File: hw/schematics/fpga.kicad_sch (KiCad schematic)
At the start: 34 parts, among them U3 ICE40UL1K-CM36AITR

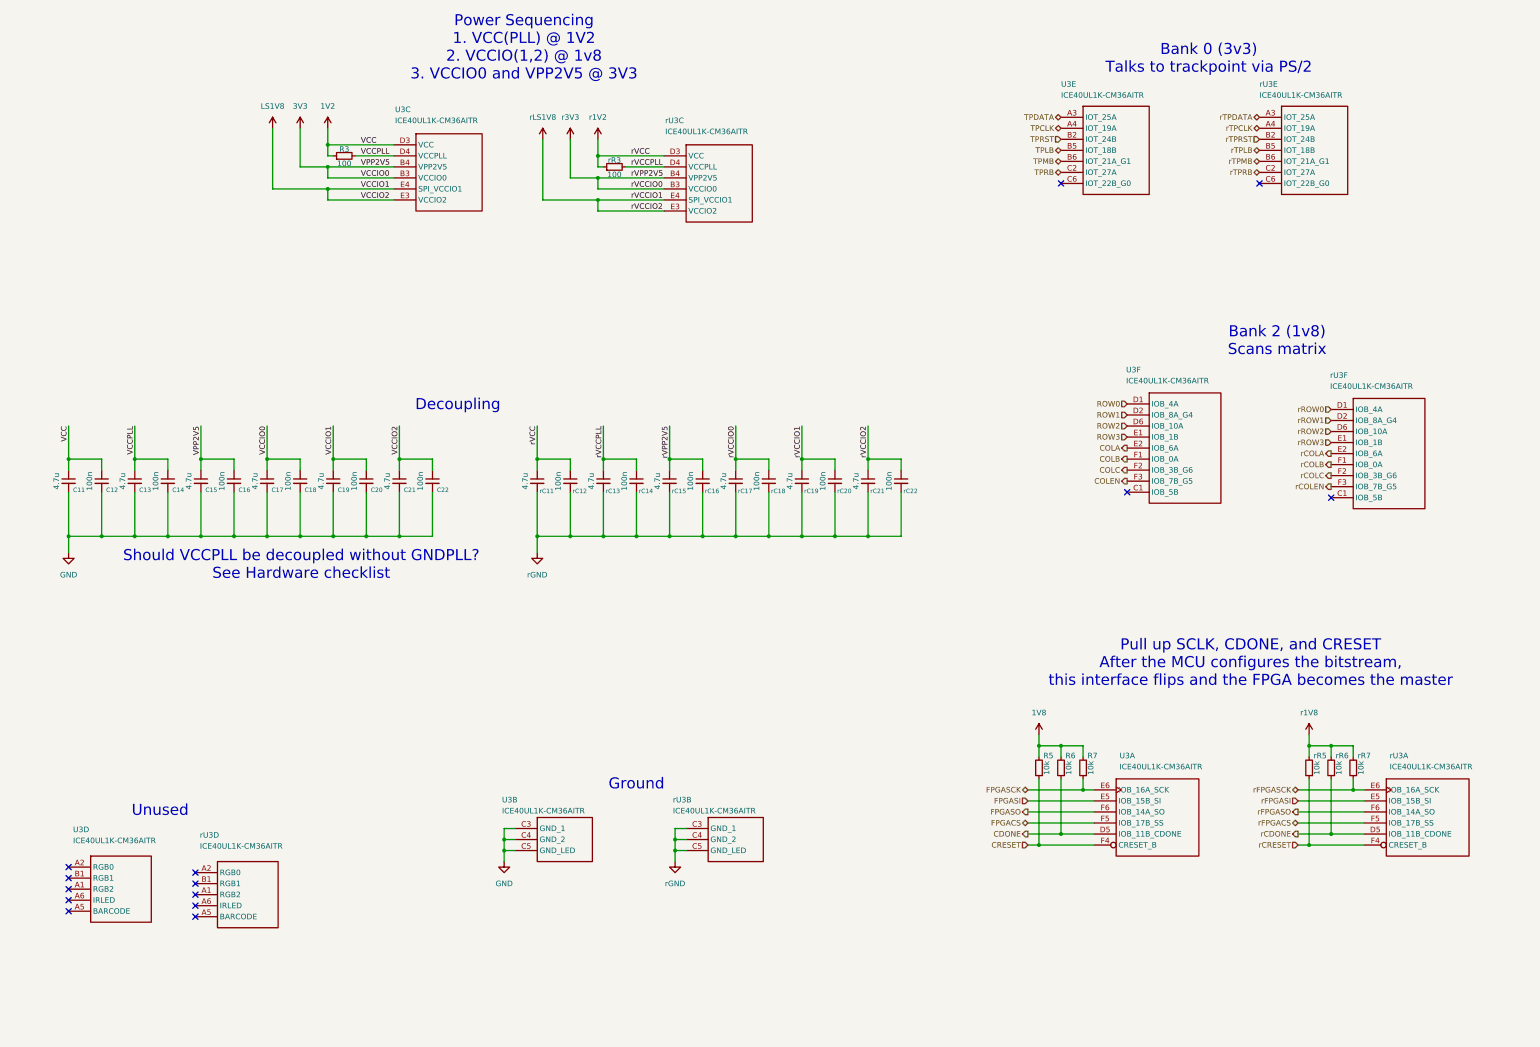
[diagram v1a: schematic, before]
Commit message: Use ICE40UP instead of UL
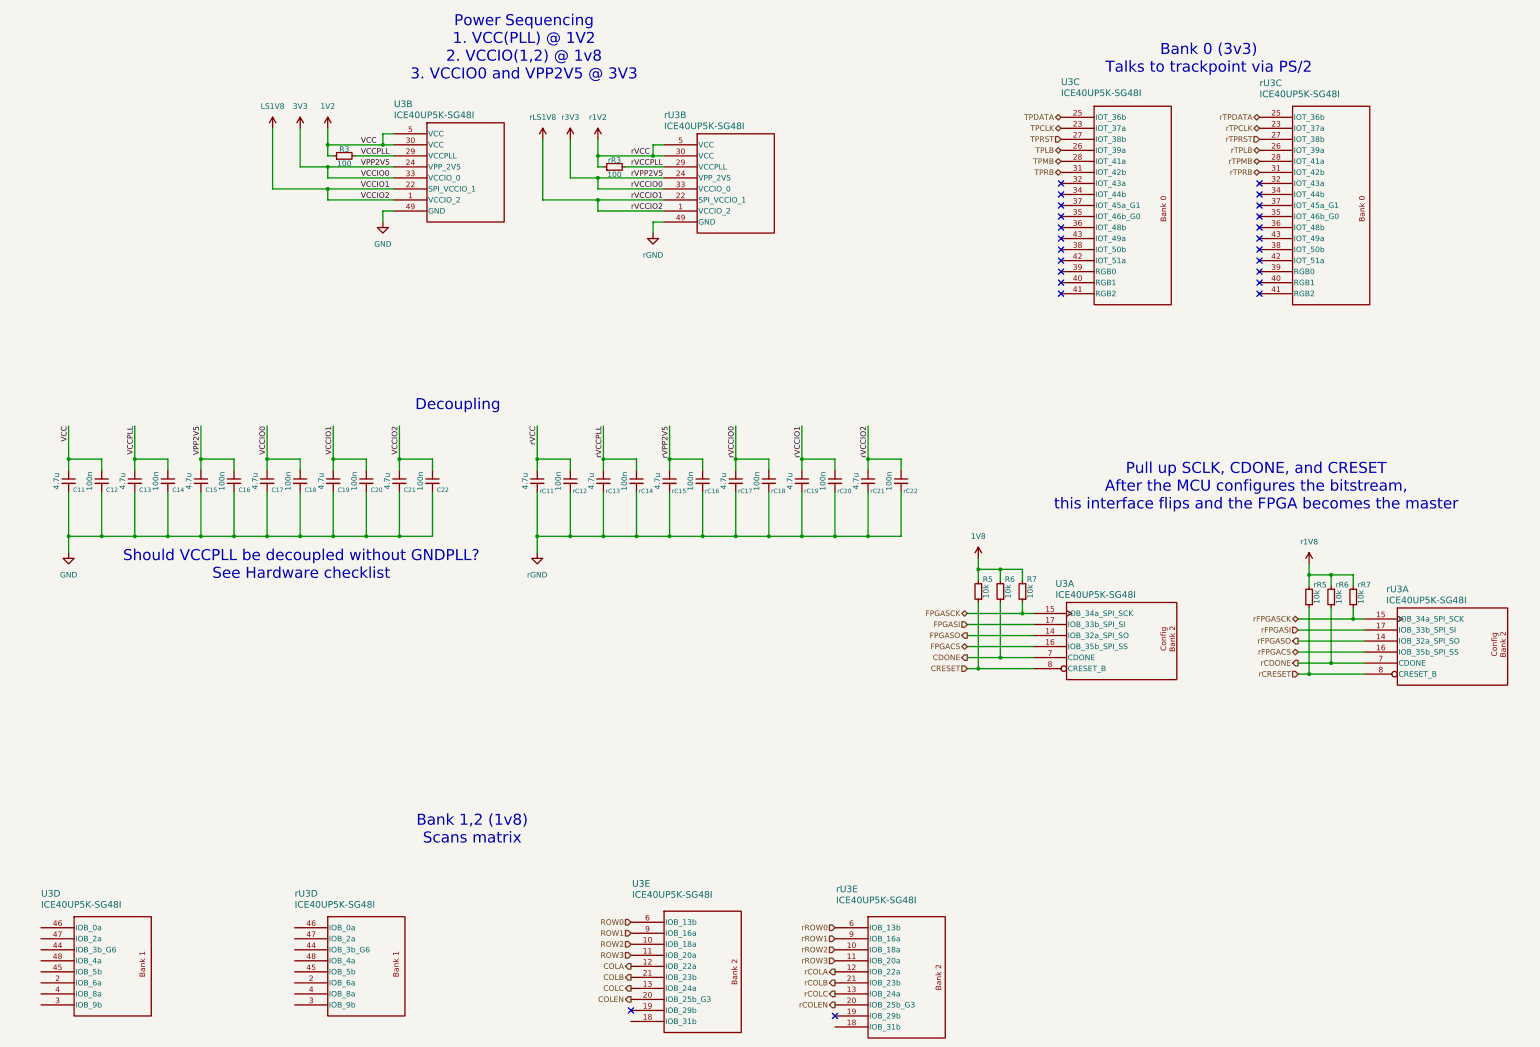
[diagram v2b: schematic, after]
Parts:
- removed U3, rU3: ICE40UL1K-CM36AITR, Alidade:BGA36C40P6X6_250X250X100, symbol Alidade:ICE40UL1K-CM36AITR
- added U3, rU3: ICE40UP5K-SG48I, Alidade:QFN48_L-ASC10_ICE40ULTRAPLUS_MACHXO2_LAT, symbol Alidade:ICE40UP5K-SG48I
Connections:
- net 1V2: now also U3.30 (VCC), U3.5 (VCC)
- net 3V3: now also U3.24 (VPP_2V5), U3.33 (VCCIO_0)
- net CDONE: now also U3.7 (CDONE)
- net COLA: now also U3.12 (IOB_22a)
- net COLB: now also U3.21 (IOB_23b)
- net COLC: now also U3.13 (IOB_24a)
- net COLEN: now also U3.20 (IOB_25b_G3)
- net CRESET: now also U3.8 (CRESET_B)
- net FPGACS: now also U3.16 (IOB_35b_SPI_SS)
- net FPGASCK: now also U3.15 (IOB_34a_SPI_SCK)
- net FPGASI: now also U3.17 (IOB_33b_SPI_SI)
- net FPGASO: now also U3.14 (IOB_32a_SPI_SO)
- net GND: now also U3.49 (GND)
- net LS1V8: now also U3.1 (VCCIO_2), U3.22 (SPI_VCCIO_1)
- net ROW0: now also U3.6 (IOB_13b)
- net ROW1: now also U3.9 (IOB_16a)
- net ROW2: now also U3.10 (IOB_18a)
- net ROW3: now also U3.11 (IOB_20a)
- net TPCLK: now also U3.23 (IOT_37a)
- net TPDATA: now also U3.25 (IOT_36b)
- net TPLB: now also U3.26 (IOT_39a)
- net TPMB: now also U3.28 (IOT_41a)
- net TPRB: now also U3.31 (IOT_42b)
- net TPRST: now also U3.27 (IOT_38b)
- net VCCPLL: now also U3.29 (VCCPLL)
- net r1V2: now also rU3.30 (VCC), rU3.5 (VCC)
- net r3V3: now also rU3.24 (VPP_2V5), rU3.33 (VCCIO_0)
- net rCDONE: now also rU3.7 (CDONE)
- net rCOLA: now also rU3.12 (IOB_22a)
- net rCOLB: now also rU3.21 (IOB_23b)
- net rCOLC: now also rU3.13 (IOB_24a)
- net rCOLEN: now also rU3.20 (IOB_25b_G3)
- net rCRESET: now also rU3.8 (CRESET_B)
- net rFPGACS: now also rU3.16 (IOB_35b_SPI_SS)
- net rFPGASCK: now also rU3.15 (IOB_34a_SPI_SCK)
- net rFPGASI: now also rU3.17 (IOB_33b_SPI_SI)
- net rFPGASO: now also rU3.14 (IOB_32a_SPI_SO)
- net rGND: now also rU3.49 (GND)
- net rLS1V8: now also rU3.1 (VCCIO_2), rU3.22 (SPI_VCCIO_1)
- net rROW0: now also rU3.6 (IOB_13b)
- net rROW1: now also rU3.9 (IOB_16a)
- net rROW2: now also rU3.10 (IOB_18a)
- net rROW3: now also rU3.11 (IOB_20a)
- net rTPCLK: now also rU3.23 (IOT_37a)
- net rTPDATA: now also rU3.25 (IOT_36b)
- net rTPLB: now also rU3.26 (IOT_39a)
- net rTPMB: now also rU3.28 (IOT_41a)
- net rTPRB: now also rU3.31 (IOT_42b)
- net rTPRST: now also rU3.27 (IOT_38b)
- net rVCCPLL: now also rU3.29 (VCCPLL)
- no-connect marks 14 -> 24
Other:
- note added: "Bank 1,2 (1v8) Scans matrix"
- note removed: "Bank 2 (1v8) Scans matrix"
- note removed: "Ground"
- note removed: "Unused"
- moved on the sheet: R5, R6, R7, rR5, rR6, rR7

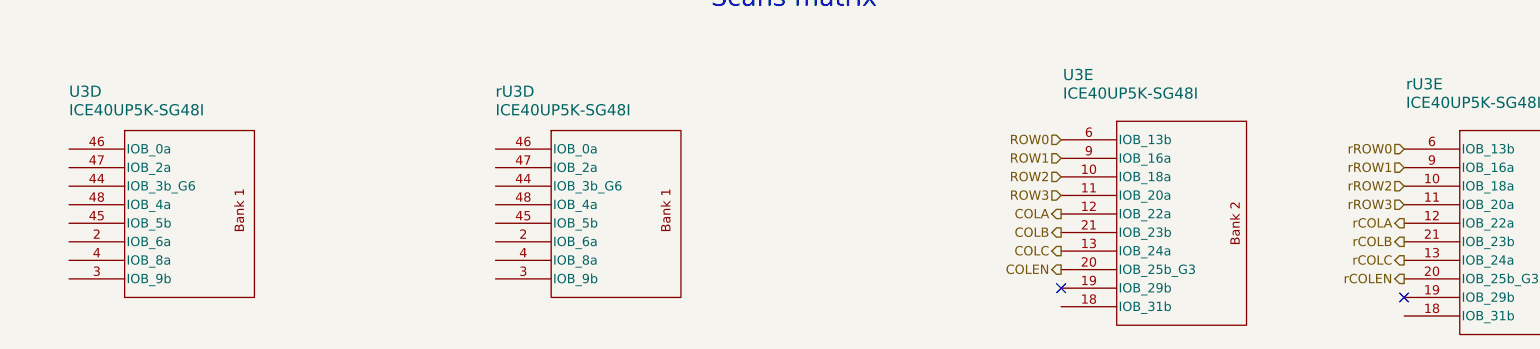
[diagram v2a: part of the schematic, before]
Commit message: Remove SN74LVC138A as we now have enough pins on the UP
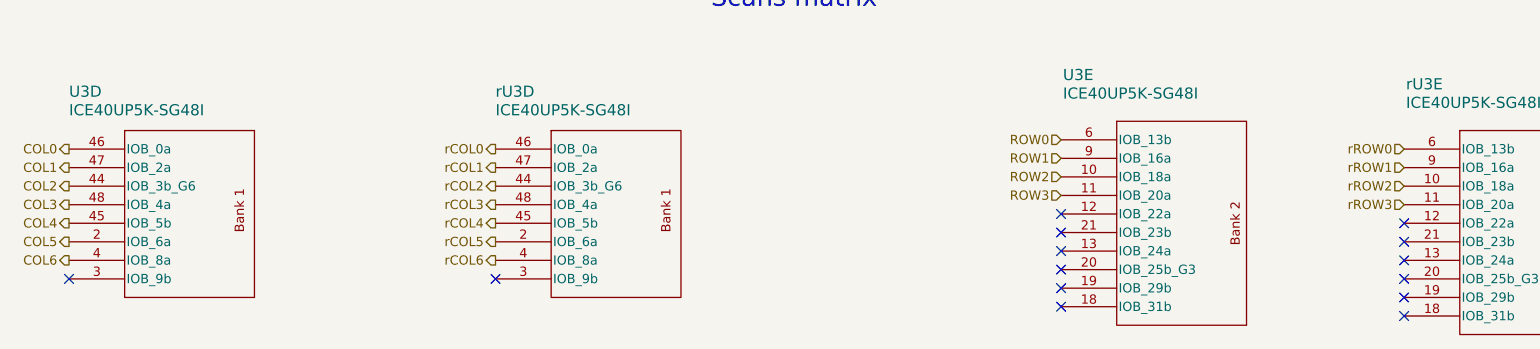
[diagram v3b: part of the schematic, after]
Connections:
- net COL5: now reaches U3.2 (IOB_6a)
- net COL6: now reaches U3.4 (IOB_8a)
- net COL2: now reaches U3.44 (IOB_3b_G6)
- net COL4: now reaches U3.45 (IOB_5b)
- net COL0: now reaches U3.46 (IOB_0a)
- net COL1: now reaches U3.47 (IOB_2a)
- net COL3: now reaches U3.48 (IOB_4a)
- net rCOL5: now reaches rU3.2 (IOB_6a)
- net rCOL6: now reaches rU3.4 (IOB_8a)
- net rCOL2: now reaches rU3.44 (IOB_3b_G6)
- net rCOL4: now reaches rU3.45 (IOB_5b)
- net rCOL0: now reaches rU3.46 (IOB_0a)
- net rCOL1: now reaches rU3.47 (IOB_2a)
- net rCOL3: now reaches rU3.48 (IOB_4a)
- net COLA: no longer names the net of U3.12 (IOB_22a)
- net COLB: no longer names the net of U3.21 (IOB_23b)
- net COLC: no longer names the net of U3.13 (IOB_24a)
- net COLEN: no longer names the net of U3.20 (IOB_25b_G3)
- net rCOLA: no longer names the net of rU3.12 (IOB_22a)
- net rCOLB: no longer names the net of rU3.21 (IOB_23b)
- net rCOLC: no longer names the net of rU3.13 (IOB_24a)
- net rCOLEN: no longer names the net of rU3.20 (IOB_25b_G3)
- no-connect marks 24 -> 36
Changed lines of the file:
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@@
+	)
+	(no_connect
+		(at 234.95 251.46)
 	)
 	(no_connect
@@
 	)
 	(no_connect
+		(at 187.96 247.65)
+	)
+	(no_connect
 		(at 332.74 85.09)
 	)
@@
 	)
 	(no_connect
+		(at 187.96 252.73)
+	)
+	(no_connect
 		(at 287.02 67.31)
 	)
 	(no_connect
+		(at 187.96 245.11)
+	)
+	(no_connect
+		(at 234.95 246.38)
+	)
+	(no_connect
 		(at 287.02 80.01)
 	)
 	(no_connect
+		(at 52.07 254)
+	)
+	(no_connect
 		(at 332.74 90.17)
 	)
 	(no_connect
+		(at 110.49 254)
+	)
+	(no_connect
+		(at 234.95 259.08)
+	)
+	(no_connect
 		(at 287.02 90.17)
 	)
@@
 	)
 	(no_connect
+		(at 234.95 254)
+	)
+	(no_connect
 		(at 332.74 69.85)
 	)
@@
 	)
 	(no_connect
+		(at 187.96 250.19)
+	)
+	(no_connect
+		(at 287.02 85.09)
+	)
+	(no_connect
+		(at 332.74 74.93)
+	)
+	(no_connect
+		(at 287.02 77.47)
+	)
+	(no_connect
+		(at 332.74 80.01)
+	)
+	(no_connect
+		(at 187.96 257.81)
+	)
+	(no_connect
 		(at 234.95 256.54)
 	)
 	(no_connect
-		(at 287.02 85.09)
-	)
-	(no_connect
-		(at 332.74 74.93)
-	)
-	(no_connect
-		(at 287.02 77.47)
-	)
-	(no_connect
-		(at 332.74 80.01)
+		(at 234.95 248.92)
 	)
 	(no_connect
@@
 			)
 			(justify right bottom)
+		)
+	)
+	(hierarchical_label "COL2"
+		(shape output)
+		(at 52.07 241.3 180)
+		(effects
+			(font
+				(size 1.27 1.27)
+			)
+			(justify right)
+		)
+	)
+	(hierarchical_label "rCOL1"
+		(shape output)
+		(at 110.49 238.76 180)
+		(effects
+			(font
+				(size 1.27 1.27)
+			)
+			(justify right)
 		)
 	)
@@
 		)
 	)
+	(hierarchical_label "rCOL3"
+		(shape output)
+		(at 110.49 243.84 180)
+		(effects
+			(font
+				(size 1.27 1.27)
+			)
+			(justify right)
+		)
+	)
 	(hierarchical_label "rTPDATA"
 		(shape bidirectional)
@@
 		)
 	)
-	(hierarchical_label "rCOLA"
+	(hierarchical_label "COL0"
 		(shape output)
-		(at 234.95 246.38 180)
-		(effects
-			(font
-				(size 1.27 1.27)
-			)
-			(justify right)
-		)
-	)
-	(hierarchical_label "COLEN"
-		(shape output)
-		(at 187.96 252.73 180)
+		(at 52.07 236.22 180)
 		(effects
 			(font
@@
 		)
 	)
+	(hierarchical_label "COL6"
+		(shape output)
+		(at 52.07 251.46 180)
+		(effects
+			(font
+				(size 1.27 1.27)
+			)
+			(justify right)
+		)
+	)
 	(hierarchical_label "TPCLK"
 		(shape bidirectional)
@@
 		)
 	)
+	(hierarchical_label "COL4"
+		(shape output)
+		(at 52.07 246.38 180)
+		(effects
+			(font
+				(size 1.27 1.27)
+			)
+			(justify right)
+		)
+	)
+	(hierarchical_label "rCOL2"
+		(shape output)
+		(at 110.49 241.3 180)
+		(effects
+			(font
+				(size 1.27 1.27)
+			)
+			(justify right)
+		)
+	)
 	(hierarchical_label "CRESET"
 		(shape input)
@@
 		)
 	)
-	(hierarchical_label "rCOLEN"
+	(hierarchical_label "COL5"
 		(shape output)
-		(at 234.95 254 180)
+		(at 52.07 248.92 180)
 		(effects
 			(font
@@
 		)
 	)
+	(hierarchical_label "COL3"
+		(shape output)
+		(at 52.07 243.84 180)
+		(effects
+			(font
+				(size 1.27 1.27)
+			)
+			(justify right)
+		)
+	)
 	(hierarchical_label "rROW0"
 		(shape input)
@@
 		)
 	)
-	(hierarchical_label "rCOLC"
+	(hierarchical_label "COL1"
 		(shape output)
-		(at 234.95 251.46 180)
+		(at 52.07 238.76 180)
 		(effects
 			(font
@@
 		)
 	)
+	(hierarchical_label "rCOL6"
+		(shape output)
+		(at 110.49 251.46 180)
+		(effects
+			(font
+				(size 1.27 1.27)
+			)
+			(justify right)
+		)
+	)
 	(hierarchical_label "TPLB"
 		(shape bidirectional)
@@
 		)
 	)
-	(hierarchical_label "COLC"
+	(hierarchical_label "rCOL4"
 		(shape output)
-		(at 187.96 250.19 180)
-		(effects
-			(font
-				(size 1.27 1.27)
-			)
-			(justify right)
-		)
-	)
-	(hierarchical_label "rCOLB"
-		(shape output)
-		(at 234.95 248.92 180)
+		(at 110.49 246.38 180)
 		(effects
 			(font
@@
 		)
 	)
-	(hierarchical_label "COLB"
-		(shape output)
-		(at 187.96 247.65 180)
-		(effects
-			(font
-				(size 1.27 1.27)
-			)
-			(justify right)
-		)
-	)
 	(hierarchical_label "TPMB"
 		(shape bidirectional)
@@
 		)
 	)
-	(hierarchical_label "COLA"
-		(shape output)
-		(at 187.96 245.11 180)
-		(effects
-			(font
-				(size 1.27 1.27)
-			)
-			(justify right)
-		)
-	)
 	(hierarchical_label "rTPLB"
 		(shape bidirectional)
@@
 		)
 	)
+	(hierarchical_label "rCOL5"
+		(shape output)
+		(at 110.49 248.92 180)
+		(effects
+			(font
+				(size 1.27 1.27)
+			)
+			(justify right)
+		)
+	)
 	(hierarchical_label "ROW3"
 		(shape input)
@@
 		(effects
 			(font
+				(size 1.27 1.27)
+			)
+			(justify right)
+		)
+	)
+	(hierarchical_label "rCOL0"
+		(shape output)
+		(at 110.49 236.22 180)
+		(effects
+			(font

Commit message: apply 0603 footprint
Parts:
- C11, C12, C13, C14, C15, C16, C17, C18, C19, C20, C21, C22, R3, R5, R6, R7, rC11, rC12, rC13, rC14, rC15, rC16, rC17, rC18, rC19, rC20, rC21, rC22, rR3, rR5, rR6, rR7: footprint (none) -> Alidade:SMD_0603
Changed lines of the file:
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@@
 			)
 		)
-		(property "Footprint" ""
+		(property "Footprint" "Alidade:SMD_0603"
 			(at 166.37 133.35 0)
 			(effects
@@
 			)
 		)
-		(property "Footprint" ""
+		(property "Footprint" "Alidade:SMD_0603"
 			(at 344.17 160.02 0)
 			(effects
@@
 			)
 		)
-		(property "Footprint" ""
+		(property "Footprint" "Alidade:SMD_0603"
 			(at 204.47 133.35 0)
 			(effects
@@
 			)
 		)
-		(property "Footprint" ""
+		(property "Footprint" "Alidade:SMD_0603"
 			(at 142.24 133.35 0)
 			(effects
@@
 			)
 		)
-		(property "Footprint" ""
+		(property "Footprint" "Alidade:SMD_0603"
 			(at 349.25 160.02 0)
 			(effects
@@
 			)
 		)
-		(property "Footprint" ""
+		(property "Footprint" "Alidade:SMD_0603"
 			(at 173.99 133.35 0)
 			(effects
@@
 			)
 		)
-		(property "Footprint" ""
+		(property "Footprint" "Alidade:SMD_0603"
 			(at 119.38 133.35 0)
 			(effects
@@
 			)
 		)
-		(property "Footprint" ""
+		(property "Footprint" "Alidade:SMD_0603"
 			(at 73.66 133.35 0)
 			(effects
@@
 			)
 		)
-		(property "Footprint" ""
+		(property "Footprint" "Alidade:SMD_0603"
 			(at 219.71 133.35 0)
 			(effects
@@
 			)
 		)
-		(property "Footprint" ""
+		(property "Footprint" "Alidade:SMD_0603"
 			(at 111.76 133.35 0)
 			(effects
@@
 			)
 		)
-		(property "Footprint" ""
+		(property "Footprint" "Alidade:SMD_0603"
 			(at 278.13 158.75 0)
 			(effects
@@
 			)
 		)
-		(property "Footprint" ""
+		(property "Footprint" "Alidade:SMD_0603"
 			(at 242.57 133.35 0)
 			(effects
@@
 			)
 		)
-		(property "Footprint" ""
+		(property "Footprint" "Alidade:SMD_0603"
 			(at 127 133.35 0)
 			(effects
@@
 			)
 		)
-		(property "Footprint" ""
+		(property "Footprint" "Alidade:SMD_0603"
 			(at 273.05 158.75 0)
 			(effects
@@
 			)
 		)
-		(property "Footprint" ""
+		(property "Footprint" "Alidade:SMD_0603"
 			(at 250.19 133.35 0)
 			(effects
@@
 			)
 		)
-		(property "Footprint" ""
+		(property "Footprint" "Alidade:SMD_0603"
 			(at 189.23 133.35 0)
 			(effects
@@
 			)
 		)
-		(property "Footprint" ""
+		(property "Footprint" "Alidade:SMD_0603"
 			(at 184.15 60.96 0)
 			(effects
@@
 			)
 		)
-		(property "Footprint" ""
+		(property "Footprint" "Alidade:SMD_0603"
 			(at 212.09 133.35 0)
 			(effects
@@
 			)
 		)
-		(property "Footprint" ""
+		(property "Footprint" "Alidade:SMD_0603"
 			(at 104.14 133.35 0)
 			(effects
@@
 			)
 		)
-		(property "Footprint" ""
+		(property "Footprint" "Alidade:SMD_0603"
 			(at 58.42 133.35 0)
 			(effects
@@
 			)
 		)
-		(property "Footprint" ""
+		(property "Footprint" "Alidade:SMD_0603"
 			(at 96.52 133.35 0)
 			(effects
@@
 			)
 		)
-		(property "Footprint" ""
+		(property "Footprint" "Alidade:SMD_0603"
 			(at 81.28 133.35 0)
 			(effects
@@
 			)
 		)
-		(property "Footprint" ""
+		(property "Footprint" "Alidade:SMD_0603"
 			(at 267.97 158.75 0)
 			(effects
@@
 			)
 		)
-		(property "Footprint" ""
+		(property "Footprint" "Alidade:SMD_0603"
 			(at 234.95 133.35 0)
 			(effects
@@
 			)
 		)
-		(property "Footprint" ""
+		(property "Footprint" "Alidade:SMD_0603"
 			(at 121.92 58.42 0)
 			(effects
@@
 			)
 		)
-		(property "Footprint" ""
+		(property "Footprint" "Alidade:SMD_0603"
 			(at 196.85 133.35 0)
 			(effects
@@
 			)
 		)
-		(property "Footprint" ""
+		(property "Footprint" "Alidade:SMD_0603"
 			(at 354.33 160.02 0)
 			(effects
@@
 			)
 		)
-		(property "Footprint" ""
+		(property "Footprint" "Alidade:SMD_0603"
 			(at 66.04 133.35 0)
 			(effects
@@
 			)
 		)
-		(property "Footprint" ""
+		(property "Footprint" "Alidade:SMD_0603"
 			(at 181.61 133.35 0)
 			(effects
@@
 			)
 		)
-		(property "Footprint" ""
+		(property "Footprint" "Alidade:SMD_0603"
 			(at 88.9 133.35 0)
 			(effects
@@
 			)
 		)
-		(property "Footprint" ""
+		(property "Footprint" "Alidade:SMD_0603"
 			(at 134.62 133.35 0)
 			(effects
@@
 			)
 		)
-		(property "Footprint" ""
+		(property "Footprint" "Alidade:SMD_0603"
 			(at 227.33 133.35 0)
 			(effects

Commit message: add some LCSC part numbers
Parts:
- U3, rU3: LCSC Part # (none) -> C2678152

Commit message: add some LCSC part numbers
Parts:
- C11, C13, C15, C17, C19, C21, rC11, rC13, rC15, rC17, rC19, rC21: footprint Alidade:SMD_0603 -> Alidade:0603; LCSC Part # (none) -> C19666
- C12, C14, C16, C18, C20, C22, rC12, rC14, rC16, rC18, rC20, rC22: footprint Alidade:SMD_0603 -> Alidade:0603; LCSC Part # (none) -> C14663
- R3, rR3: footprint Alidade:SMD_0603 -> Alidade:0603; LCSC Part # (none) -> C22775
- R5, R6, R7, rR5, rR6, rR7: footprint Alidade:SMD_0603 -> Alidade:0603; LCSC Part # (none) -> C25804
